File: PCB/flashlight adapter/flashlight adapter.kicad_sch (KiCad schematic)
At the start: 15 parts, among them J1 USB4105-GF-A, U1 MIC2295YD5-TR, U3 BQ24074RGT, U4 DW01A

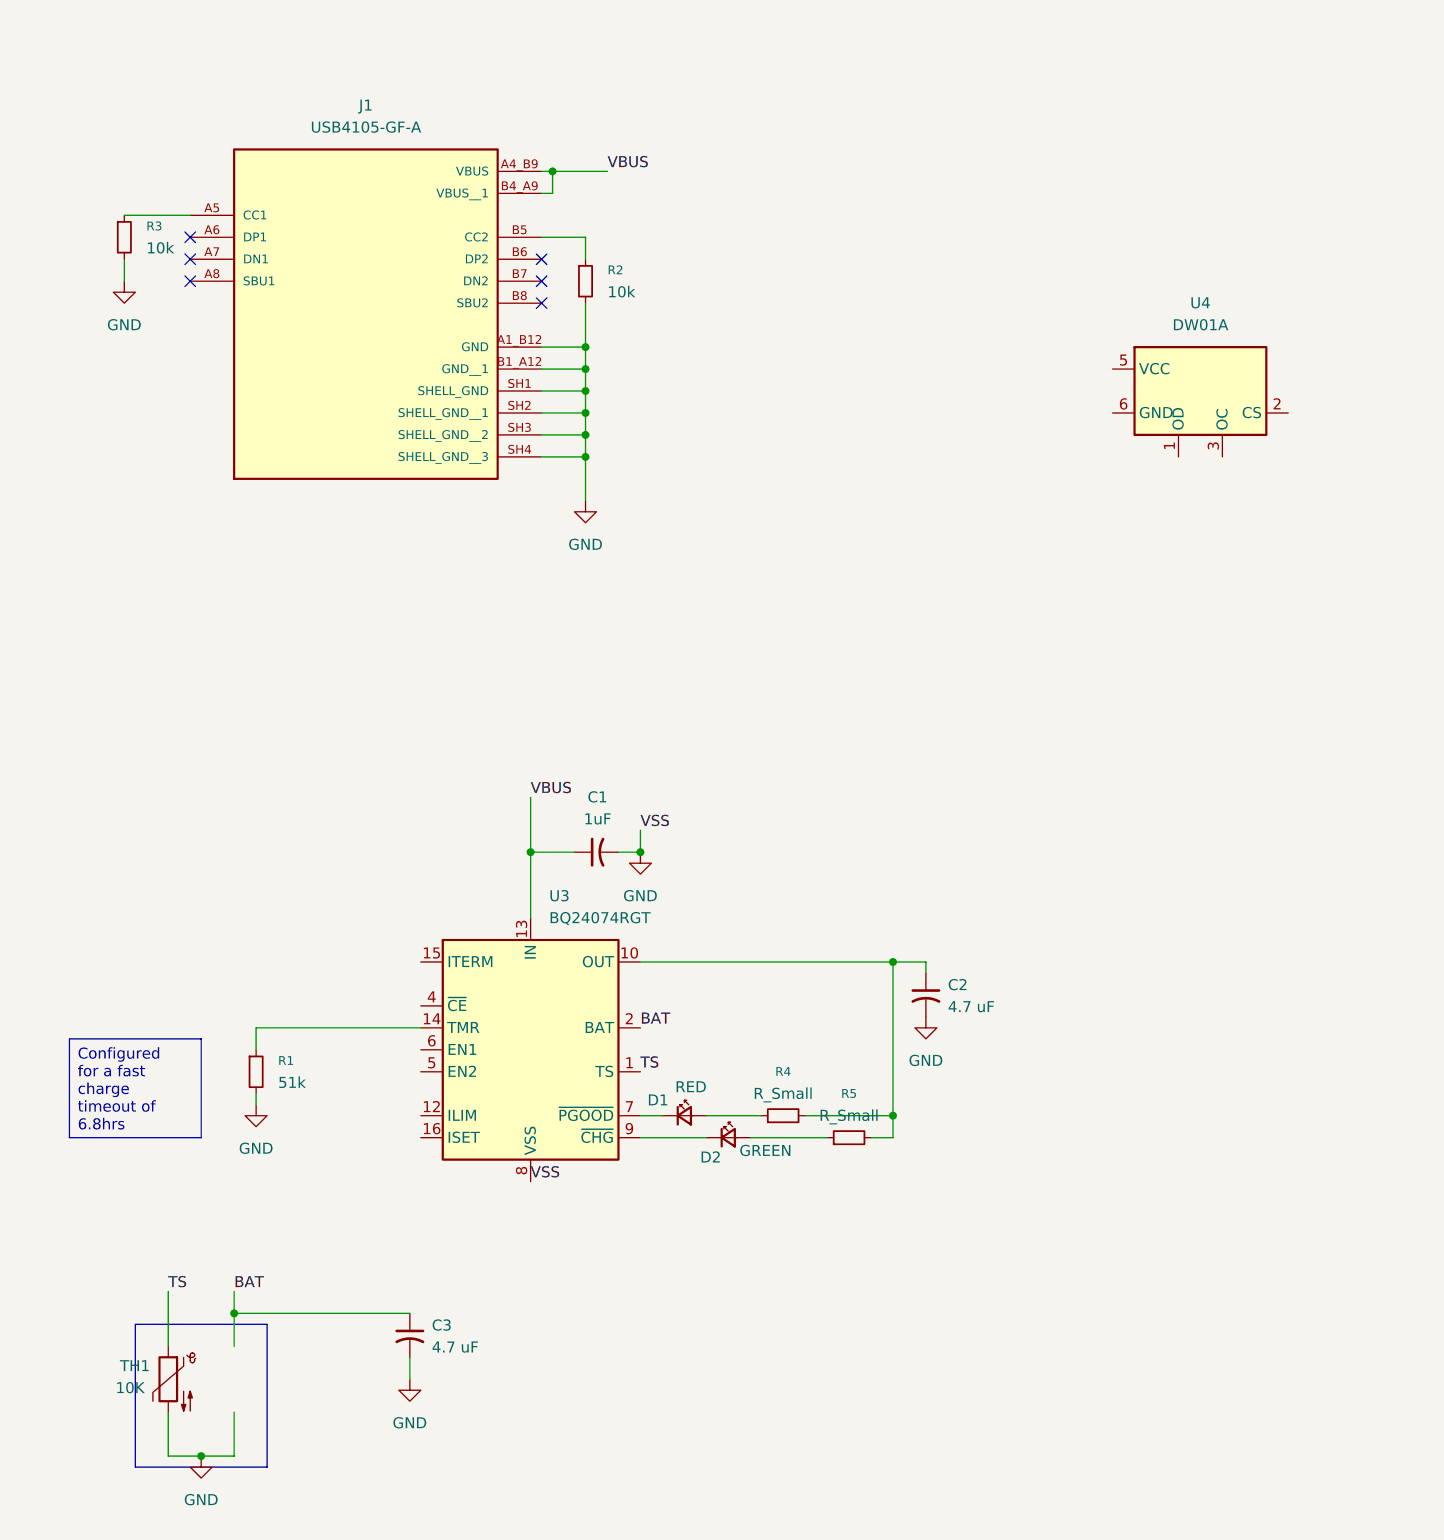
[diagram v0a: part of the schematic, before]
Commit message: Completed Charging IC schematic
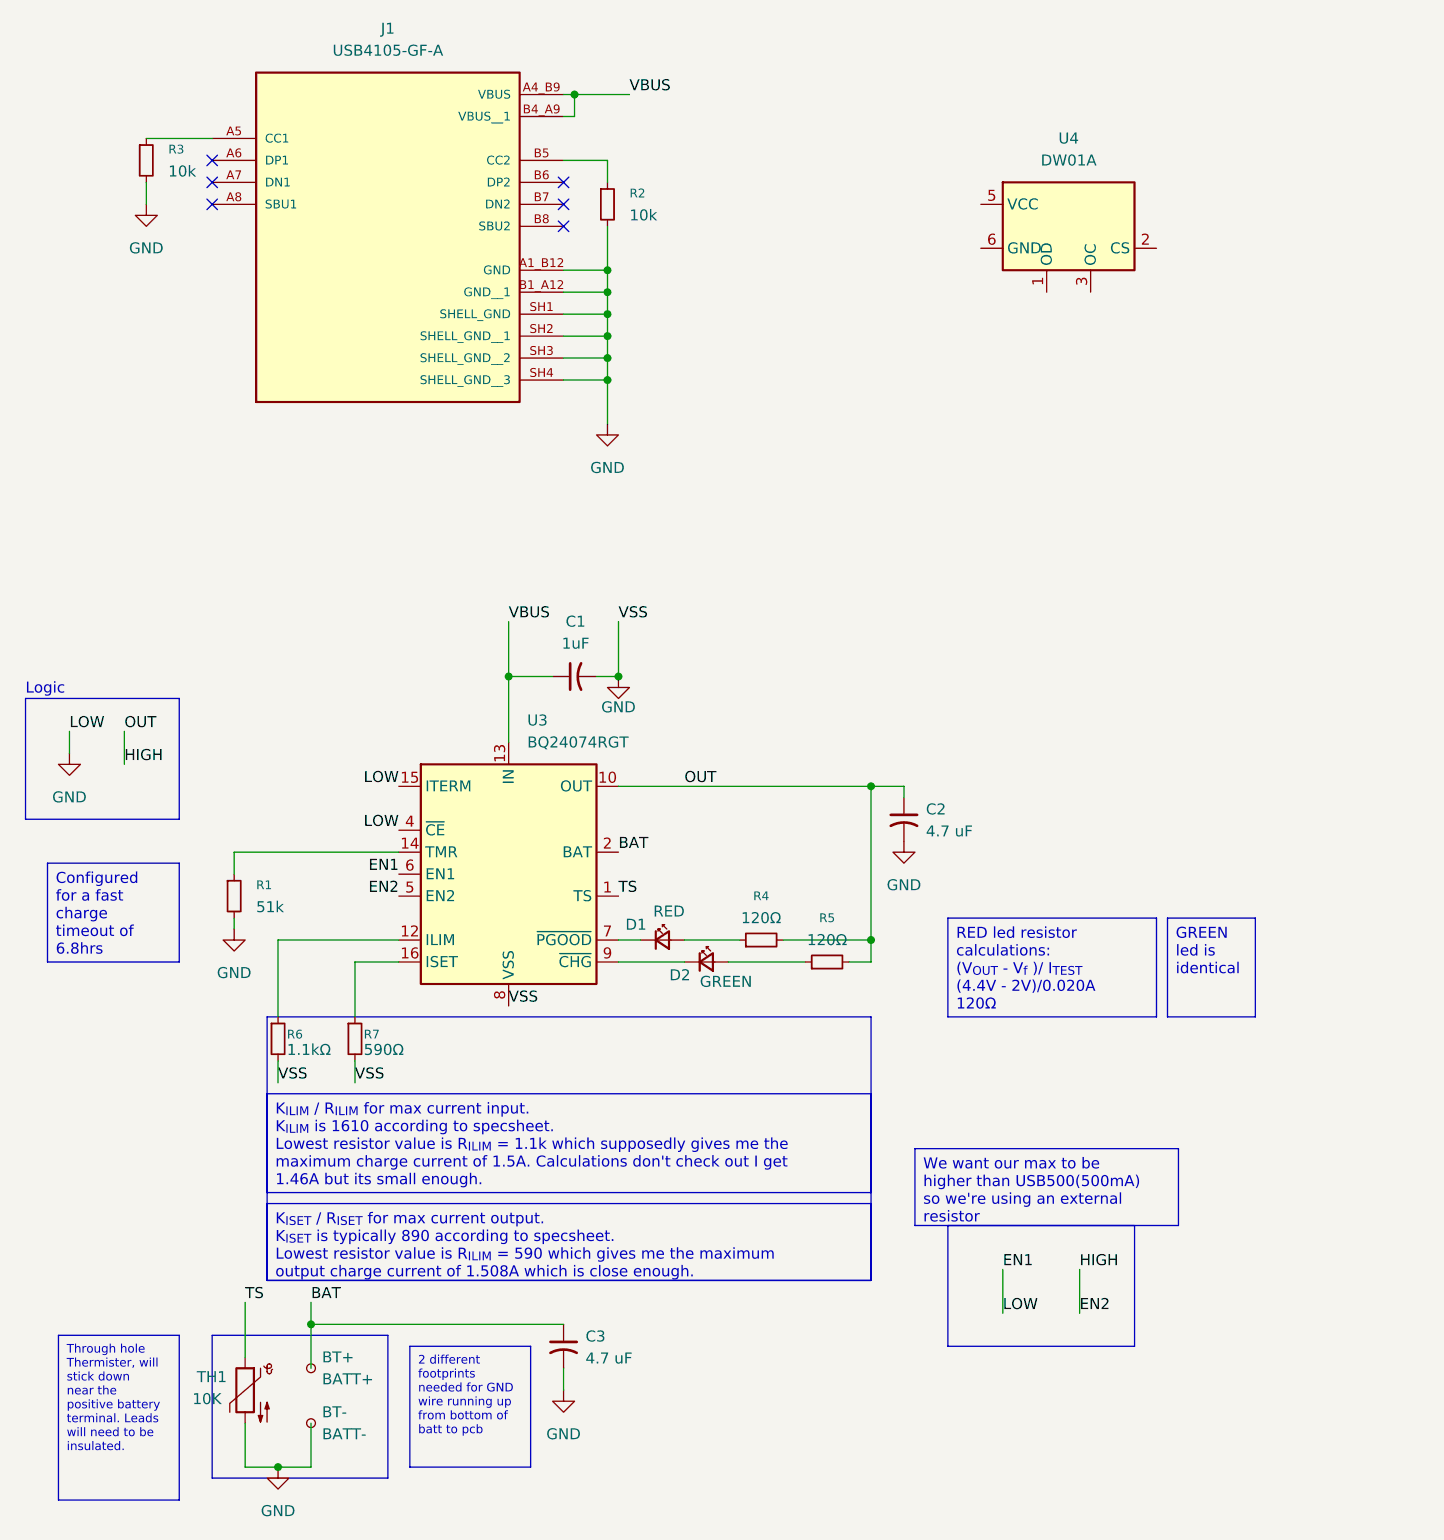
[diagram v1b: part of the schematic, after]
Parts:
- added BT+: BATT+, symbol Connector:TestPoint_Small
- added BT-: BATT-, symbol Connector:TestPoint_Small
- added R6: 1.1kΩ, Resistor_SMD:R_0603_1608Metric_Pad0.98x0.95mm_HandSolder, symbol Device:R_Small
- added R7: 590Ω, Resistor_SMD:R_0603_1608Metric_Pad0.98x0.95mm_HandSolder, symbol Device:R_Small
- D1, D2: footprint (none) -> LED_SMD:LED_0603_1608Metric_Pad1.05x0.95mm_HandSolder
- R4, R5: value R_Small -> 120Ω; footprint (none) -> Resistor_SMD:R_0603_1608Metric_Pad0.98x0.95mm_HandSolder
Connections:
- net BAT: now also BT+.1
- net GND: now also U3.15 (ITERM), U3.4 (~{CE}), U3.6 (EN1), BT-.1, R6.2, R7.2
- net EN2: now reaches C2.1, R4.2, R5.2, U3.10 (OUT), U3.11 (OUT)
- net EN2: now also U3.5 (EN2)
- net at U3.12 (ILIM): now also R6.1
- net at U3.16 (ISET): now also R7.1
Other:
- note added: "Logic"
- moved on the sheet: C1, C2, C3, D1, J1, R1, R2, R3, R4, TH1, U3, U4

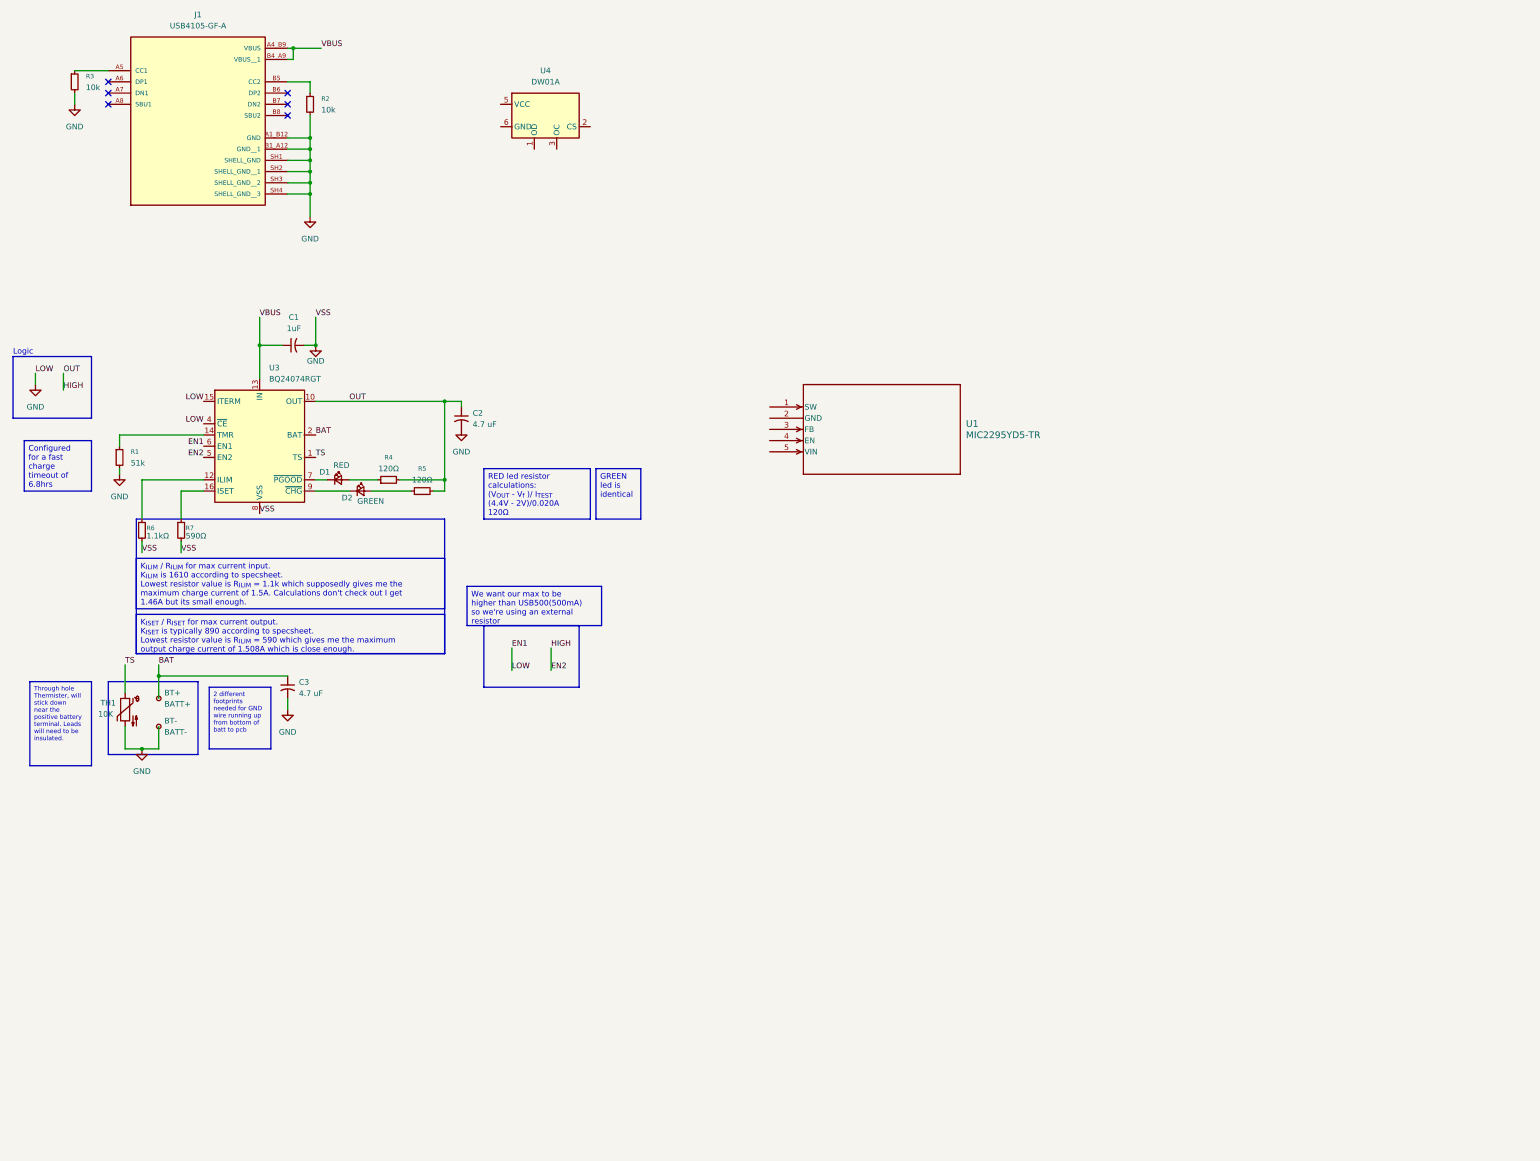
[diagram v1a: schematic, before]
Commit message: finished low voltage cutoff ic
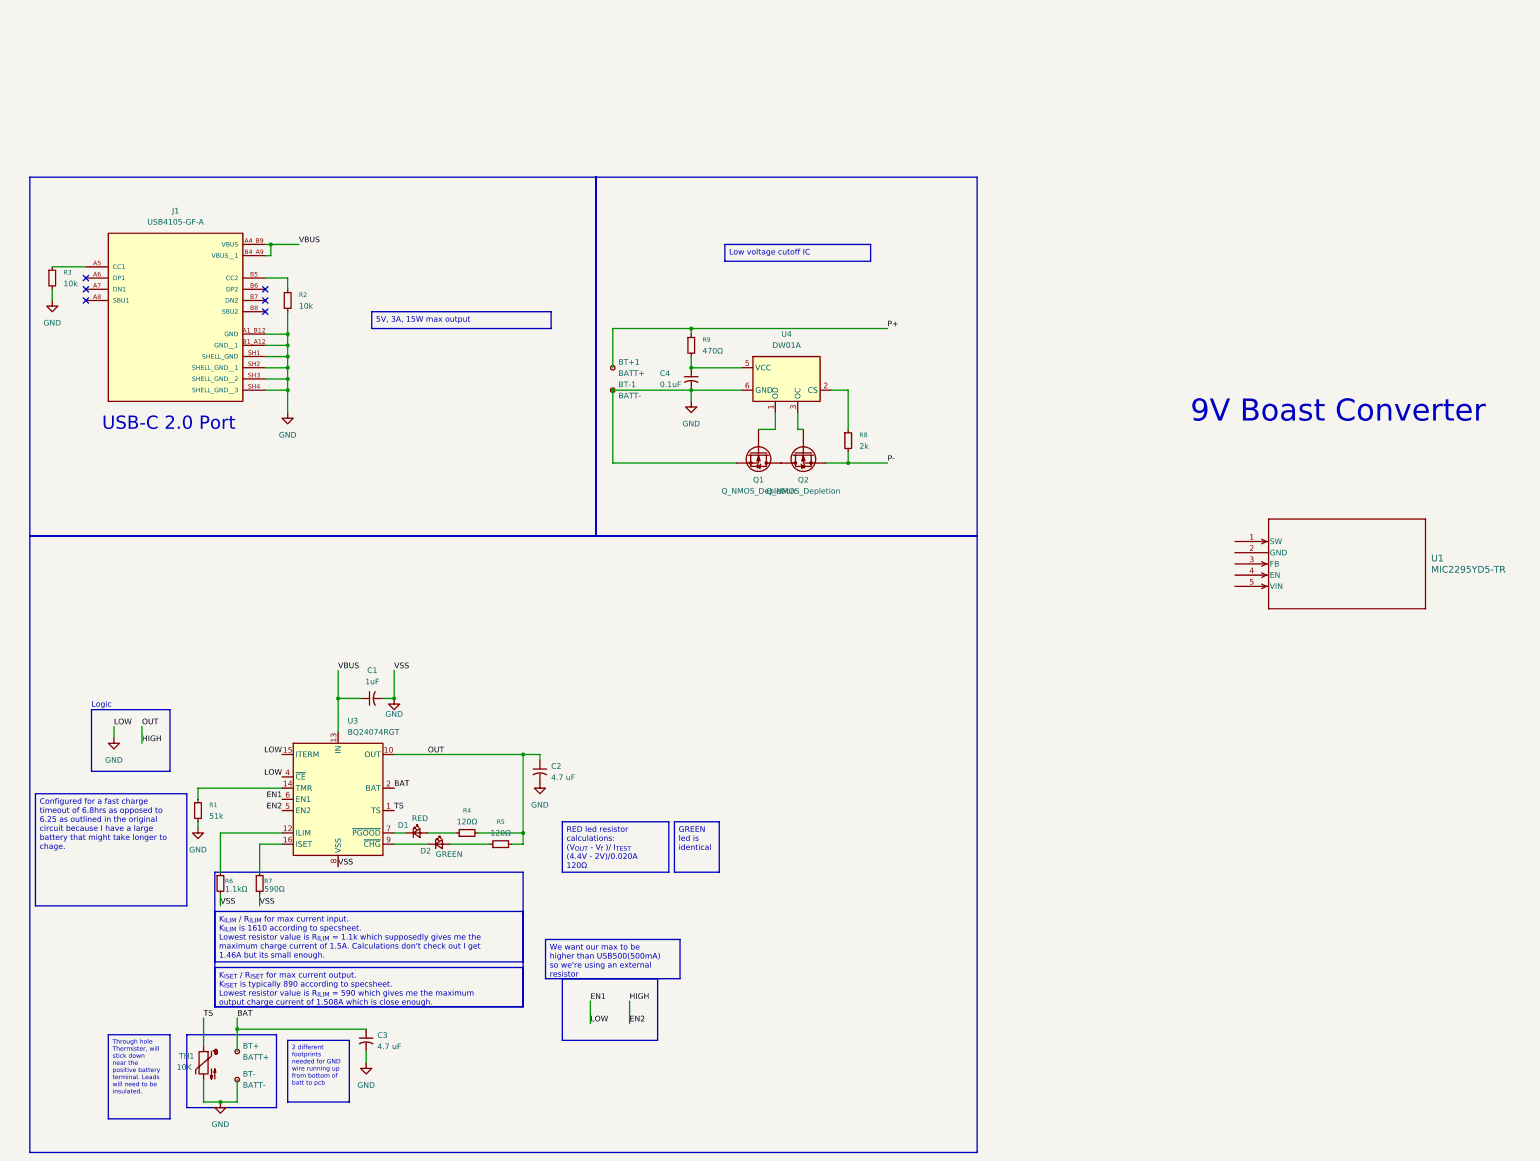
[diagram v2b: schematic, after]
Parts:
- added BT+1: BATT+, symbol Connector:TestPoint_Small
- added BT-1: BATT-, symbol Connector:TestPoint_Small
- added C4: 0.1uF, Capacitor_SMD:C_0603_1608Metric_Pad1.08x0.95mm_HandSolder, symbol Device:C_Small_US
- added Q1, Q2: Q_NMOS_Depletion, symbol Device:Q_NMOS_Depletion
- added R8: 2k, Resistor_SMD:R_0603_1608Metric_Pad0.98x0.95mm_HandSolder, symbol Device:R_Small
- added R9: 470Ω, Resistor_SMD:R_0603_1608Metric_Pad0.98x0.95mm_HandSolder, symbol Device:R_Small
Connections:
- net GND: now also U4.6 (GND), BT-1.1, C4.2, Q1.S
- net at U4.1 (OD): now also Q1.G
- net at U4.2 (CS): now also R8.1
- net at U4.3 (OC): now also Q2.G
- net at U4.5 (VCC): now also C4.1, R9.2
- new net: Q1.D, Q2.D
- new net P+: BT+1.1, R9.1
- new net P-: Q2.S, R8.2
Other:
- note added: "9V Boast Converter"
- note added: "USB-C 2.0 Port"
- moved on the sheet: BT+, BT-, C1, C2, C3, D1, D2, J1, R1, R2, R3, R4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
